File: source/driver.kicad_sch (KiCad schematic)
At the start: 68 parts, among them P1 SWD, P10 SWD, P2 SWD, P3 SWD, P4 SWD, P5 SWD, P6 SWD, P7 SWD, P8 SWD, P9 SWD, SW2 SW_DPDT_x2, U3 AMS1117-3.3, U4 IRS21867S, U5 XL1509-5.0E1, U6 IRS21867S, U7 IRS21867S, U8 TX4130L/PW2902

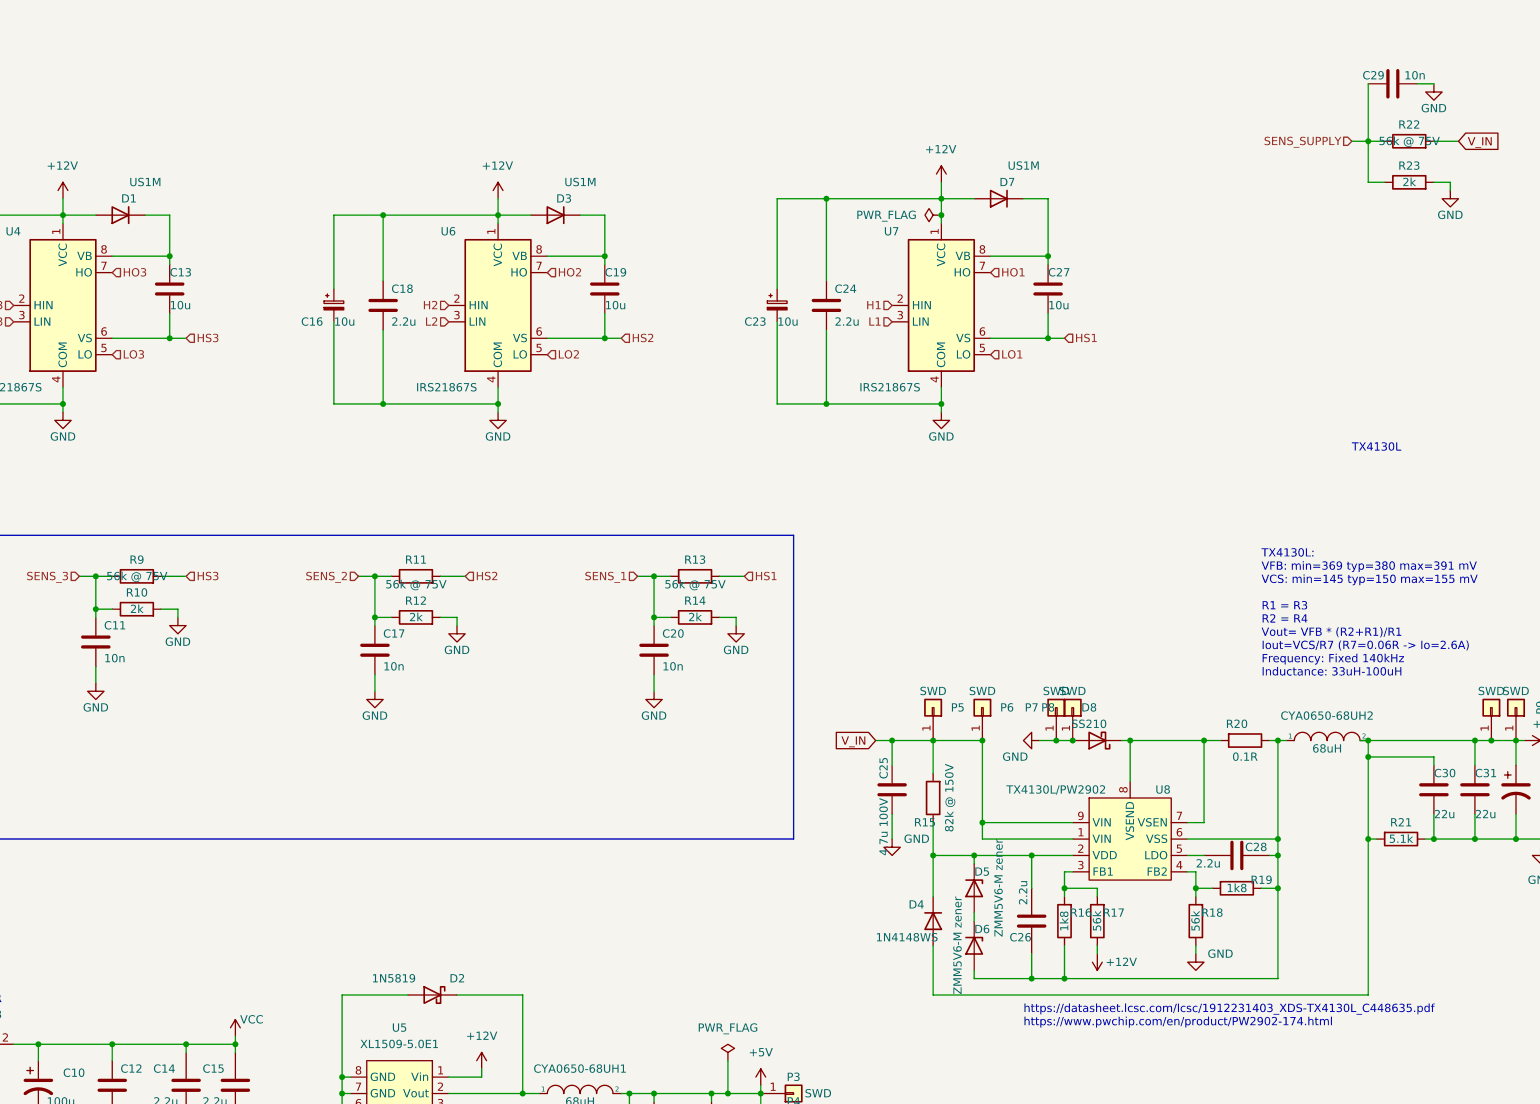
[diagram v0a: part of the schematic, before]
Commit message: Add files via upload
Added six pull down resistors to mosfet gates, and removed 100 pF filter caps on current samplings. Changed Logo back to FOC-king. This is a potential release candidates - everything works, also HFI. Have not yet verified NRF though.
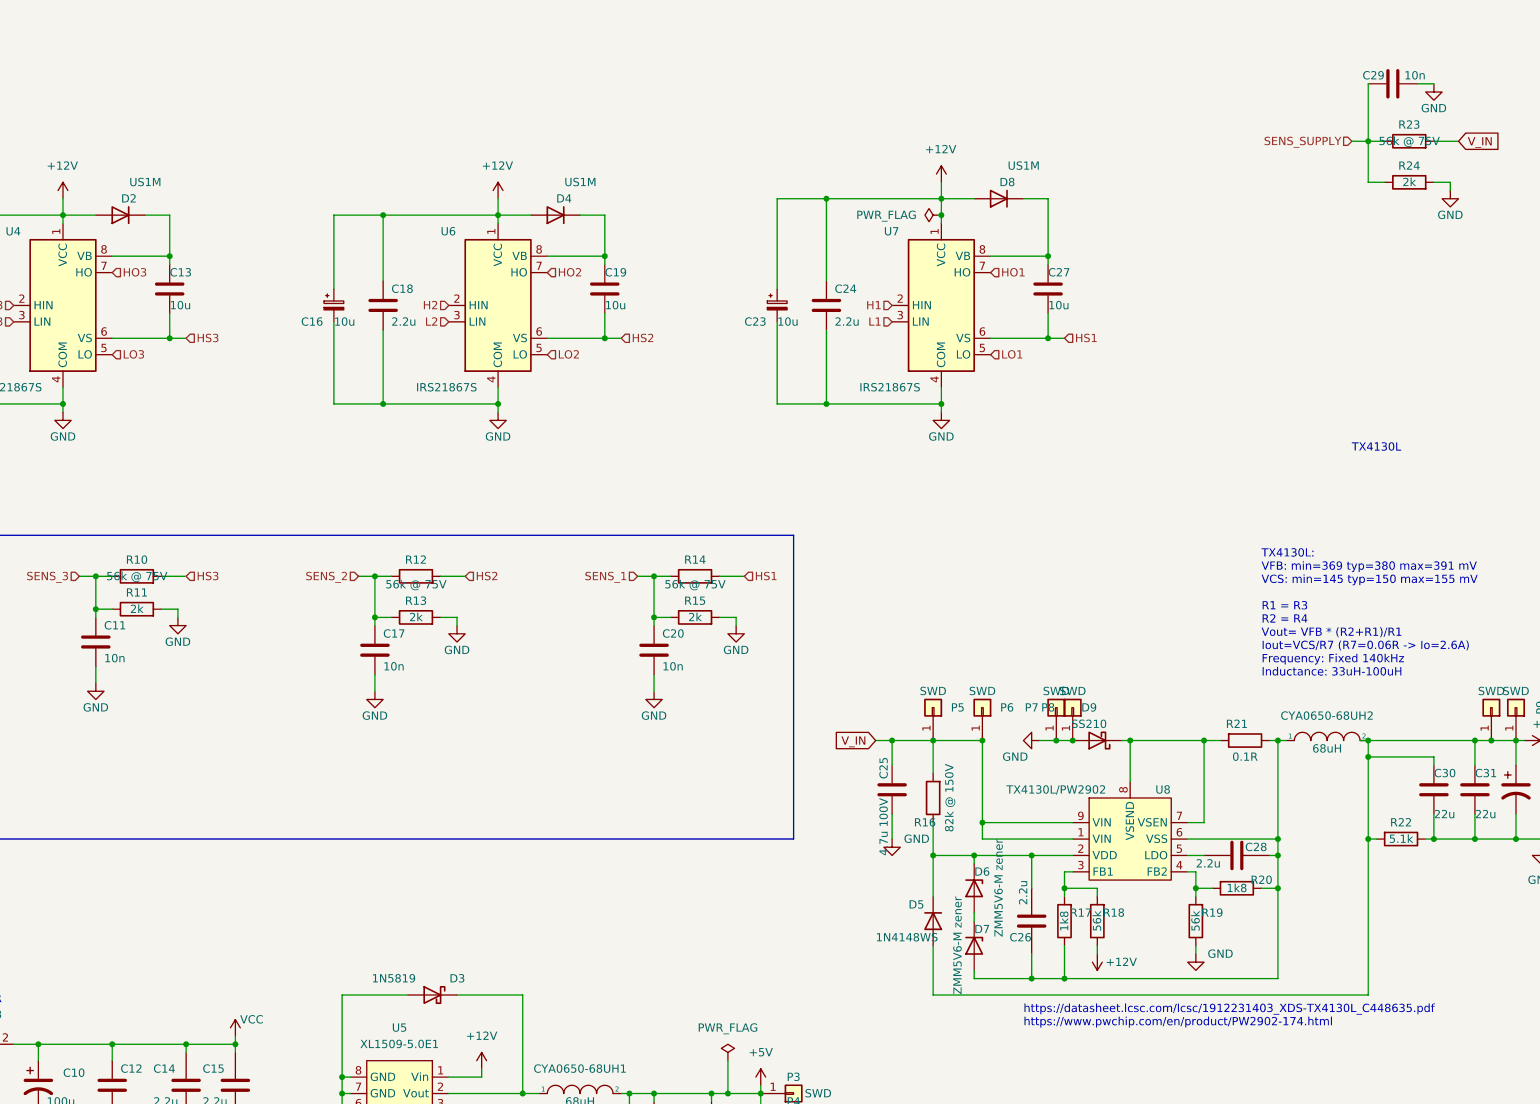
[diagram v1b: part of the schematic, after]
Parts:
- renumbered D1 to D2, D2 to D3, D3 to D4, D4 to D5, D5 to D6, D6 to D7, D7 to D8, D8 to D9, R9 to R10, R10 to R11, R11 to R12, R12 to R13, R13 to R14, R14 to R15, R15 to R16, R16 to R17, R17 to R18, R18 to R19, R19 to R20, R20 to R21, R21 to R22, R22 to R23, R23 to R24

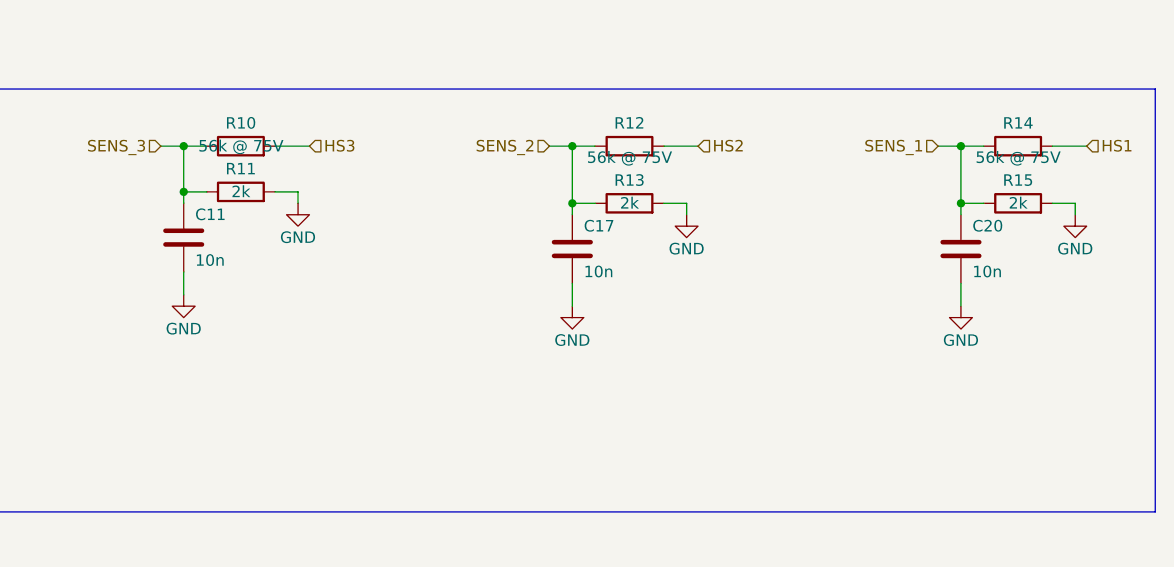
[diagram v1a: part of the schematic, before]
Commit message: Moved traces to make peripherals work
PPM now works -> moved trace to PB7
UART works -> connected PB10 and PB11 to Communication port (like vesc 75_300 UART)
Removed NRF24 pinheader
Added motor_temperature to Hall pinheader, like it should be
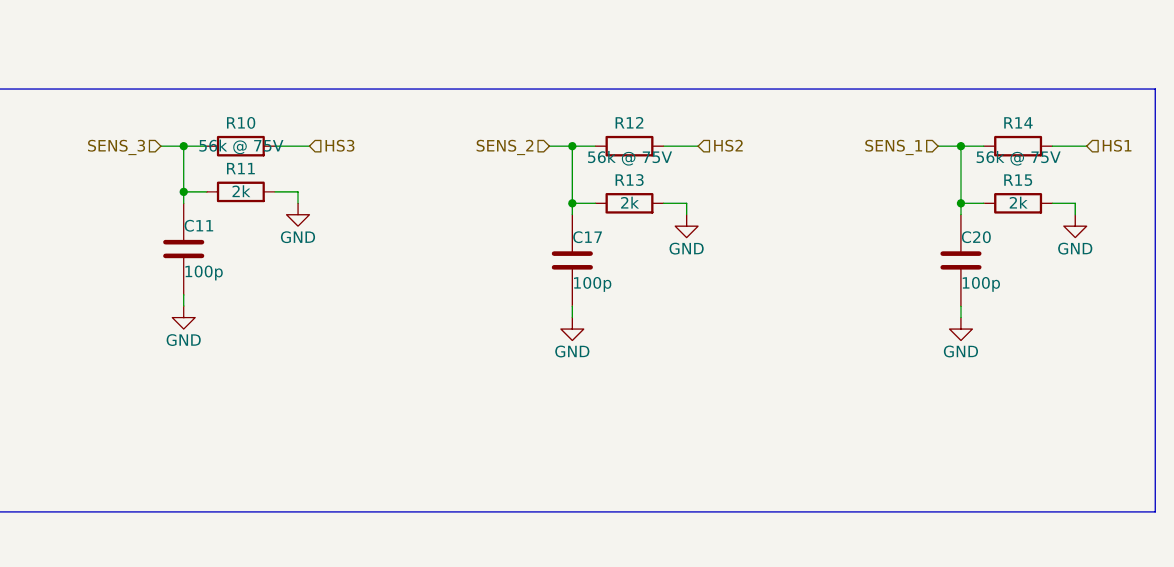
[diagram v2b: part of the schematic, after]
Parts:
- removed C11, C17, C20: 10n, Capacitor_SMD:C_0603_1608Metric, symbol Device:C
- added C11, C17, C20: 100p, Capacitor_SMD:C_0603_1608Metric, symbol BLDC_4-rescue:C-RESCUE-BLDC_4
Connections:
- net GND: now also C11.1, C17.1, C20.1
- net SENS_1: now also C20.2
- net SENS_2: now also C17.2
- net SENS_3: now also C11.2
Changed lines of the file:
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@@
     (stroke (width 0) (type default) (color 0 0 0 0))
   )
-  (wire (pts (xy 100.33 110.49) (xy 100.33 113.03))
-    (stroke (width 0) (type default) (color 0 0 0 0))
-  )
   (wire (pts (xy 195.58 45.72) (xy 204.47 45.72))
     (stroke (width 0) (type default) (color 0 0 0 0))
@@
     (stroke (width 0) (type default) (color 0 0 0 0))
   )
+  (wire (pts (xy 100.33 114.3) (xy 100.33 113.03))
+    (stroke (width 0) (type default) (color 0 0 0 0))
+  )
   (wire (pts (xy 212.09 144.78) (xy 212.09 143.51))
     (stroke (width 0) (type default) (color 0 0 0 0))
@@
     (stroke (width 0) (type default) (color 0 0 0 0))
   )
+  (wire (pts (xy 57.15 113.03) (xy 57.15 111.76))
+    (stroke (width 0) (type default) (color 0 0 0 0))
+  )
   (wire (pts (xy 180.34 120.65) (xy 180.34 124.46))
     (stroke (width 0) (type default) (color 0 0 0 0))
@@
     (stroke (width 0) (type default) (color 0 0 0 0))
   )
+  (wire (pts (xy 143.51 114.3) (xy 143.51 113.03))
+    (stroke (width 0) (type default) (color 0 0 0 0))
+  )
   (wire (pts (xy 127 45.72) (xy 135.89 45.72))
     (stroke (width 0) (type default) (color 0 0 0 0))
@@
     (stroke (width 0) (type default) (color 0 0 0 0))
   )
-  (wire (pts (xy 143.51 110.49) (xy 143.51 113.03))
-    (stroke (width 0) (type default) (color 0 0 0 0))
-  )
   (wire (pts (xy 100.33 101.6) (xy 100.33 102.87))
     (stroke (width 0) (type default) (color 0 0 0 0))
@@
     (stroke (width 0) (type default) (color 0 0 0 0))
   )
-  (wire (pts (xy 57.15 109.22) (xy 57.15 111.76))
-    (stroke (width 0) (type default) (color 0 0 0 0))
-  )
   (wire (pts (xy 186.69 160.02) (xy 254 160.02))
     (stroke (width 0) (type default) (color 0 0 0 0))
@@
     (pin "9")
   )
-  (symbol (lib_id "Device:C") (at 100.33 106.68 0) (unit 1)
-    (in_bom yes) (on_board yes)
-    (property "Reference" "C17" (id 0) (at 101.6 104.14 0)
-      (effects (font (size 1.27 1.27)) (justify left))
-    )
-    (property "Value" "10n" (id 1) (at 101.6 109.22 0)
-      (effects (font (size 1.27 1.27)) (justify left))
-    )
-    (property "Footprint" "Capacitor_SMD:C_0603_1608Metric" (id 2) (at 101.2952 110.49 0)
-      (effects (font (size 1.27 1.27)) hide)
-    )
-    (property "Datasheet" "~" (id 3) (at 100.33 106.68 0)
-      (effects (font (size 1.27 1.27)) hide)
-    )
-    (property "LCSC" "C57112" (id 4) (at 100.33 106.68 0)
-      (effects (font (size 1.27 1.27)) hide)
-    )
-    (pin "1")
-    (pin "2")
-  )
   (symbol (lib_id "BLDC_4-rescue:C-RESCUE-BLDC_4") (at 71.12 173.99 0) (unit 1)
     (in_bom yes) (on_board yes)
@@
     (pin "2")
   )
+  (symbol (lib_id "BLDC_4-rescue:C-RESCUE-BLDC_4") (at 57.15 106.68 0) (mirror x) (unit 1)
+    (in_bom yes) (on_board yes)
+    (property "Reference" "C11" (id 0) (at 57.15 104.14 0)
+      (effects (font (size 1.27 1.27)) (justify left))
+    )
+    (property "Value" "100p" (id 1) (at 57.15 109.22 0)
+      (effects (font (size 1.27 1.27)) (justify left))
+    )
+    (property "Footprint" "Capacitor_SMD:C_0603_1608Metric" (id 2) (at 57.15 106.68 0)
+      (effects (font (size 1.524 1.524)) hide)
+    )
+    (property "Datasheet" "" (id 3) (at 57.15 106.68 0)
+      (effects (font (size 1.524 1.524)) hide)
+    )
+    (property "LCSC" "C14858" (id 4) (at 57.15 106.68 0)
+      (effects (font (size 1.27 1.27)) hide)
+    )
+    (pin "1")
+    (pin "2")
+  )
   (symbol (lib_id "power:GND") (at 78.74 181.61 0) (unit 1)
     (in_bom yes) (on_board yes) (fields_autoplaced)
@@
     (pin "1")
   )
-  (symbol (lib_id "power:GND") (at 100.33 113.03 0) (unit 1)
+  (symbol (lib_id "BLDC_4-rescue:C-RESCUE-BLDC_4") (at 143.51 107.95 0) (mirror x) (unit 1)
+    (in_bom yes) (on_board yes)
+    (property "Reference" "C20" (id 0) (at 143.51 105.41 0)
+      (effects (font (size 1.27 1.27)) (justify left))
+    )
+    (property "Value" "100p" (id 1) (at 143.51 110.49 0)
+      (effects (font (size 1.27 1.27)) (justify left))
+    )
+    (property "Footprint" "Capacitor_SMD:C_0603_1608Metric" (id 2) (at 143.51 107.95 0)
+      (effects (font (size 1.524 1.524)) hide)
+    )
+    (property "Datasheet" "" (id 3) (at 143.51 107.95 0)
+      (effects (font (size 1.524 1.524)) hide)
+    )
+    (property "LCSC" "C14858" (id 4) (at 143.51 107.95 0)
+      (effects (font (size 1.27 1.27)) hide)
+    )
+    (pin "1")
+    (pin "2")
+  )
+  (symbol (lib_id "power:GND") (at 100.33 114.3 0) (unit 1)
     (in_bom yes) (on_board yes)
-    (property "Reference" "#PWR027" (id 0) (at 100.33 119.38 0)
+    (property "Reference" "#PWR027" (id 0) (at 100.33 120.65 0)
       (effects (font (size 1.27 1.27)) hide)
     )
-    (property "Value" "GND" (id 1) (at 100.33 116.84 0))
-    (property "Footprint" "" (id 2) (at 100.33 113.03 0)
+    (property "Value" "GND" (id 1) (at 100.33 118.11 0))
+    (property "Footprint" "" (id 2) (at 100.33 114.3 0)
       (effects (font (size 1.27 1.27)) hide)
     )
-    (property "Datasheet" "" (id 3) (at 100.33 113.03 0)
+    (property "Datasheet" "" (id 3) (at 100.33 114.3 0)
       (effects (font (size 1.27 1.27)) hide)
     )
@@
     (pin "2")
   )
+  (symbol (lib_id "BLDC_4-rescue:C-RESCUE-BLDC_4") (at 100.33 107.95 0) (mirror x) (unit 1)
+    (in_bom yes) (on_board yes)
+    (property "Reference" "C17" (id 0) (at 100.33 105.41 0)
+      (effects (font (size 1.27 1.27)) (justify left))
+    )
+    (property "Value" "100p" (id 1) (at 100.33 110.49 0)
+      (effects (font (size 1.27 1.27)) (justify left))
+    )
+    (property "Footprint" "Capacitor_SMD:C_0603_1608Metric" (id 2) (at 100.33 107.95 0)
+      (effects (font (size 1.524 1.524)) hide)
+    )
+    (property "Datasheet" "" (id 3) (at 100.33 107.95 0)
+      (effects (font (size 1.524 1.524)) hide)
+    )
+    (property "LCSC" "C14858" (id 4) (at 100.33 107.95 0)
+      (effects (font (size 1.27 1.27)) hide)
+    )
+    (pin "1")
+    (pin "2")
+  )
   (symbol (lib_id "Diode:1N4148W") (at 128.27 39.37 180) (unit 1)
     (in_bom yes) (on_board yes)
@@
     (pin "8")
   )
-  (symbol (lib_id "power:GND") (at 57.15 111.76 0) (unit 1)
+  (symbol (lib_id "power:GND") (at 57.15 113.03 0) (unit 1)
     (in_bom yes) (on_board yes)
-    (property "Reference" "#PWR023" (id 0) (at 57.15 118.11 0)
+    (property "Reference" "#PWR023" (id 0) (at 57.15 119.38 0)
       (effects (font (size 1.27 1.27)) hide)
     )
-    (property "Value" "GND" (id 1) (at 57.15 115.57 0))
-    (property "Footprint" "" (id 2) (at 57.15 111.76 0)
+    (property "Value" "GND" (id 1) (at 57.15 116.84 0))
+    (property "Footprint" "" (id 2) (at 57.15 113.03 0)
       (effects (font (size 1.27 1.27)) hide)
     )
-    (property "Datasheet" "" (id 3) (at 57.15 111.76 0)
+    (property "Datasheet" "" (id 3) (at 57.15 113.03 0)
       (effects (font (size 1.27 1.27)) hide)
     )
@@
     (pin "1")
   )
-  (symbol (lib_id "Device:C") (at 143.51 106.68 0) (unit 1)
-    (in_bom yes) (on_board yes)
-    (property "Reference" "C20" (id 0) (at 144.78 104.14 0)
-      (effects (font (size 1.27 1.27)) (justify left))
-    )
-    (property "Value" "10n" (id 1) (at 144.78 109.22 0)
-      (effects (font (size 1.27 1.27)) (justify left))
-    )
-    (property "Footprint" "Capacitor_SMD:C_0603_1608Metric" (id 2) (at 144.4752 110.49 0)
-      (effects (font (size 1.27 1.27)) hide)
-    )
-    (property "Datasheet" "~" (id 3) (at 143.51 106.68 0)
-      (effects (font (size 1.27 1.27)) hide)
-    )
-    (property "LCSC" "C57112" (id 4) (at 143.51 106.68 0)
-      (effects (font (size 1.27 1.27)) hide)
-    )
-    (pin "1")
-    (pin "2")
-  )
   (symbol (lib_id "Device:R") (at 207.01 148.59 180) (unit 1)
     (in_bom yes) (on_board yes)
@@
     (pin "2")
   )
-  (symbol (lib_id "power:GND") (at 143.51 113.03 0) (unit 1)
+  (symbol (lib_id "power:GND") (at 143.51 114.3 0) (unit 1)
     (in_bom yes) (on_board yes)
-    (property "Reference" "#PWR033" (id 0) (at 143.51 119.38 0)
+    (property "Reference" "#PWR033" (id 0) (at 143.51 120.65 0)
       (effects (font (size 1.27 1.27)) hide)
     )
-    (property "Value" "GND" (id 1) (at 143.51 116.84 0))
-    (property "Footprint" "" (id 2) (at 143.51 113.03 0)
+    (property "Value" "GND" (id 1) (at 143.51 118.11 0))
+    (property "Footprint" "" (id 2) (at 143.51 114.3 0)
       (effects (font (size 1.27 1.27)) hide)
     )
-    (property "Datasheet" "" (id 3) (at 143.51 113.03 0)
+    (property "Datasheet" "" (id 3) (at 143.51 114.3 0)
       (effects (font (size 1.27 1.27)) hide)
     )
@@
     (pin "1")
   )
-  (symbol (lib_id "Device:C") (at 57.15 105.41 0) (unit 1)
-    (in_bom yes) (on_board yes)
-    (property "Reference" "C11" (id 0) (at 58.42 102.87 0)
-      (effects (font (size 1.27 1.27)) (justify left))
-    )
-    (property "Value" "10n" (id 1) (at 58.42 107.95 0)
-      (effects (font (size 1.27 1.27)) (justify left))
-    )
-    (property "Footprint" "Capacitor_SMD:C_0603_1608Metric" (id 2) (at 58.1152 109.22 0)
-      (effects (font (size 1.27 1.27)) hide)
-    )
-    (property "Datasheet" "~" (id 3) (at 57.15 105.41 0)
-      (effects (font (size 1.27 1.27)) hide)
-    )
-    (property "LCSC" "C57112" (id 4) (at 57.15 105.41 0)
-      (effects (font (size 1.27 1.27)) hide)
-    )
-    (pin "1")
-    (pin "2")
-  )
   (symbol (lib_id "power:GND") (at 118.11 193.04 0) (unit 1)

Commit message: Momentary switch
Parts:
- removed C21: 100u, Capacitor_Tantalum_SMD:CP_EIA-3528-21_Kemet-B, symbol Custom_Library:C_T491D107K016AT
- removed C30: 22u, Capacitor_SMD:C_0805_2012Metric, symbol Device:C
- removed D7: ZMM5V6-M zener, Diode_SMD:D_MiniMELF, symbol Diode:BZX384-xxx
- added C8: 47u, Capacitor_SMD:C_0805_2012Metric, symbol Device:C
- added D1: SS34, Diode_SMD:D_SMA, symbol Device:D_Schottky
- added J5: on/off, Connector_JST:JST_PH_B4B-PH-K_1x04_P2.00mm_Vertical, symbol Connector_Generic:Conn_01x04
- added Q1: AO3401A, Package_TO_SOT_SMD:SOT-23, symbol Transistor_FET:AO3401A
- added Q2, Q3: SS8050, Package_TO_SOT_SMD:SOT-23, symbol Transistor_BJT:MMBT3904
- added R10, R13: 10k, Resistor_SMD:R_0603_1608Metric, symbol Device:R
- added R11: 10M, Resistor_SMD:R_0603_1608Metric, symbol Device:R
- added R12, R8, R9: 75k, Resistor_SMD:R_0603_1608Metric, symbol Device:R
- D6: value ZMM5V6-M zener -> MM1W18 1W18V zener; footprint Diode_SMD:D_MiniMELF -> Diode_SMD:D_SOD-123; LCSC C8062 -> C382948
- SW2: footprint Jumper:SolderJumper-2_P1.3mm_Bridged_Pad1.0x1.5mm -> Jumper:SolderJumper-2_P1.3mm_Open_Pad1.0x1.5mm
- renumbered C8 to C10, C9 to C11, C11 to C12, C12 to C13, C13 to C14, C14 to C15, C15 to C16, C16 to C17, C17 to C18, C18 to C19, C19 to C20, C10 to C21, C20 to C22, C22 to C23, C23 to C24, C24 to C25, C25 to C26, C26 to C27, C27 to C28, C28 to C29, C29 to C30, C7 to C9, D8 to D7, D9 to D8, P10 to P1, P9 to P10, P1 to P2, P2 to P3, P3 to P4, P4 to P5, P5 to P6, P6 to P7, P7 to P8, P8 to P9, R10 to R14, R11 to R15, R12 to R16, R13 to R17, R14 to R18, R15 to R19, R16 to R20, R17 to R21, R18 to R22, R19 to R23, R20 to R24, R21 to R25, R22 to R26, R23 to R27, R24 to R28
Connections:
- net +12V: now also Q1.2 (S), R12.2, R8.2; no longer P1.1 (Pin_1), U5.1 (Vin)
- net +5V: now also C21.1
- net GND: now also SW2.1 (A), U5.4 (O/O), C8.2, Q2.2 (E), Q3.2 (E), R10.2, R13.1; no longer SW2.2 (B)
- net H1: now also U4.2 (HIN); no longer U7.2 (HIN)
- net H3: now also U7.2 (HIN); no longer U4.2 (HIN)
- net HO1: now also U4.7 (HO); no longer U7.7 (HO)
- net HO3: now also U7.7 (HO); no longer U4.7 (HO)
- net HS1: now also C14.2, R14.2, U4.6 (VS); no longer C28.2, R18.2, U7.6 (VS)
- net HS3: now also C28.2, R18.2, U7.6 (VS); no longer C14.2, R14.2, U4.6 (VS)
- net L1: now also U4.3 (LIN); no longer U7.3 (LIN)
- net L3: now also U7.3 (LIN); no longer U4.3 (LIN)
- net LO1: now also U4.5 (LO); no longer U7.5 (LO)
- net LO3: now also U7.5 (LO); no longer U4.5 (LO)
- net SENS_1: now also C12.2, R14.1, R15.1; no longer C22.2, R18.1, R19.1
- net SENS_3: now also C22.2, R18.1, R19.1; no longer C12.2, R14.1, R15.1
- net VCC: no longer C21.1
- net at C27.1, C29.1, CYA0650-68UH2.1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: now also D6.2 (A)
- new net: Q1.1 (G), Q2.3 (C), R8.1, SW2.2 (B)
- new net: J5.2 (Pin_2), Q3.3 (C), R12.1
- new net: D1.2 (A), Q1.3 (D), R11.2, R13.2, R9.2
- new net: C8.1, Q3.1 (B), R11.1
- new net: J5.1 (Pin_1), Q2.1 (B), R9.1
- new net: J5.3 (Pin_3), R10.1
- new net: D1.1 (K), J5.4 (Pin_4), P1.1 (Pin_1), U5.1 (Vin)
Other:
- note added: "Latch Circuit: https://electronoobs.com/eng_circuitos_tut60.php"
- note added: "https://www.youtube.com/watch?v=Foc9R0dC2iI"
- note added: "pulldown resistor needed due to diode"
- moved on the sheet: C21, C23, D6, P1
